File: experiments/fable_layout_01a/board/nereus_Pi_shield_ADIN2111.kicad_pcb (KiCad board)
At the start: 6 copper layers, 46 x 65 mm, 138 parts, among them J1 Raspberry_Pi_2_3, J5 SM02B-GHS-TB, T1 74930000, T2 74930000, U1 ADIN2111BCPZ, U10 LMR51430YDDCR, U11 TPS26621DRCR, U2 AP22913CN4-7, U3 AP22913CN4-7, U4 INA232AIDDFR, U5 LMR51430YDDCR, U6 TPS62840YBGR, Y1 ABM11W-25.0000MHZ-6-K1Z-T3

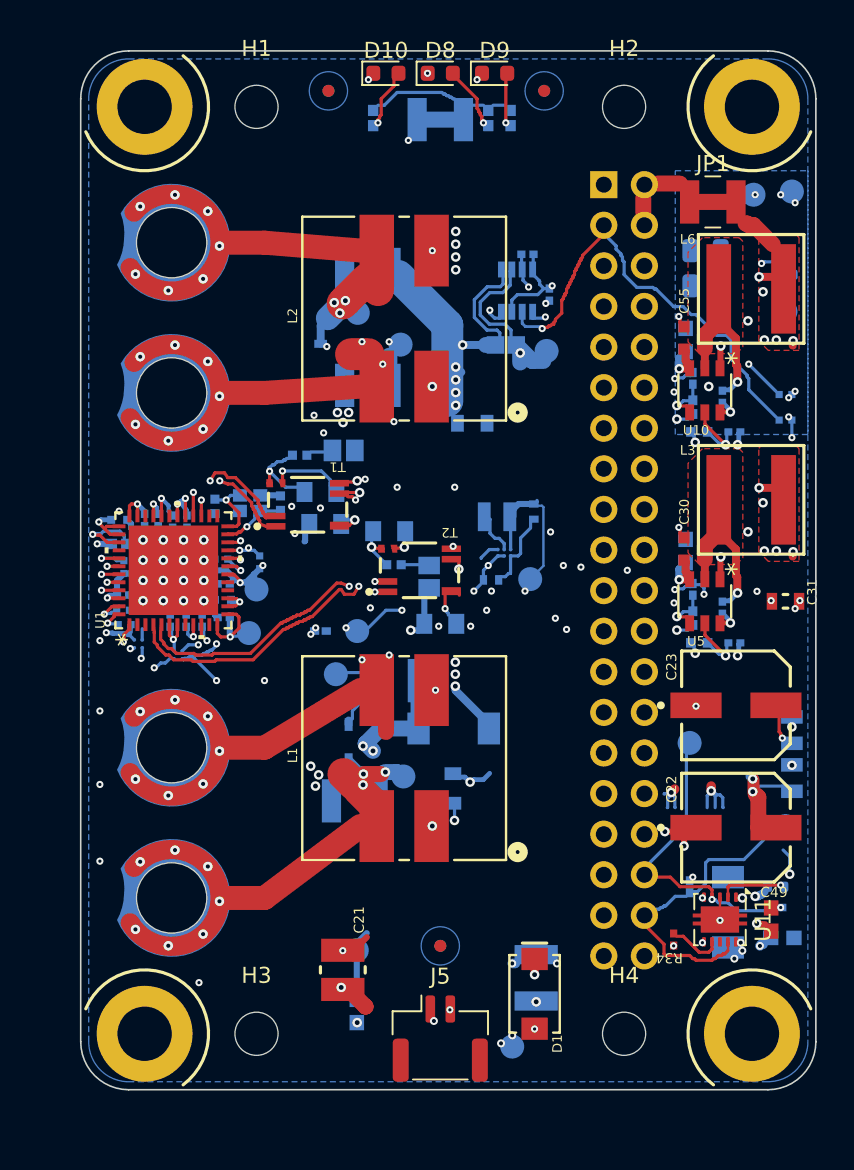
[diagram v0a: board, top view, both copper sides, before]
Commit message: fable layout 1.a S2.b: board 49 x 68 (width west, height south), inserts 1.5 mm nearer the wall, U1 pocket (centre tried in 8 trials: OPTIONS A3), SPI first on an Internal 2 lane, straightened pairs 9.39/8.77/19.93/20.61, jumpers on top at the north edge, JLCPCB DFM 30/31, DRC 109 (all Sofar's) / 70, review + before/after pages, REPORT
Co-Authored-By: Claude Fable 5.1 <noreply@anthropic.com>
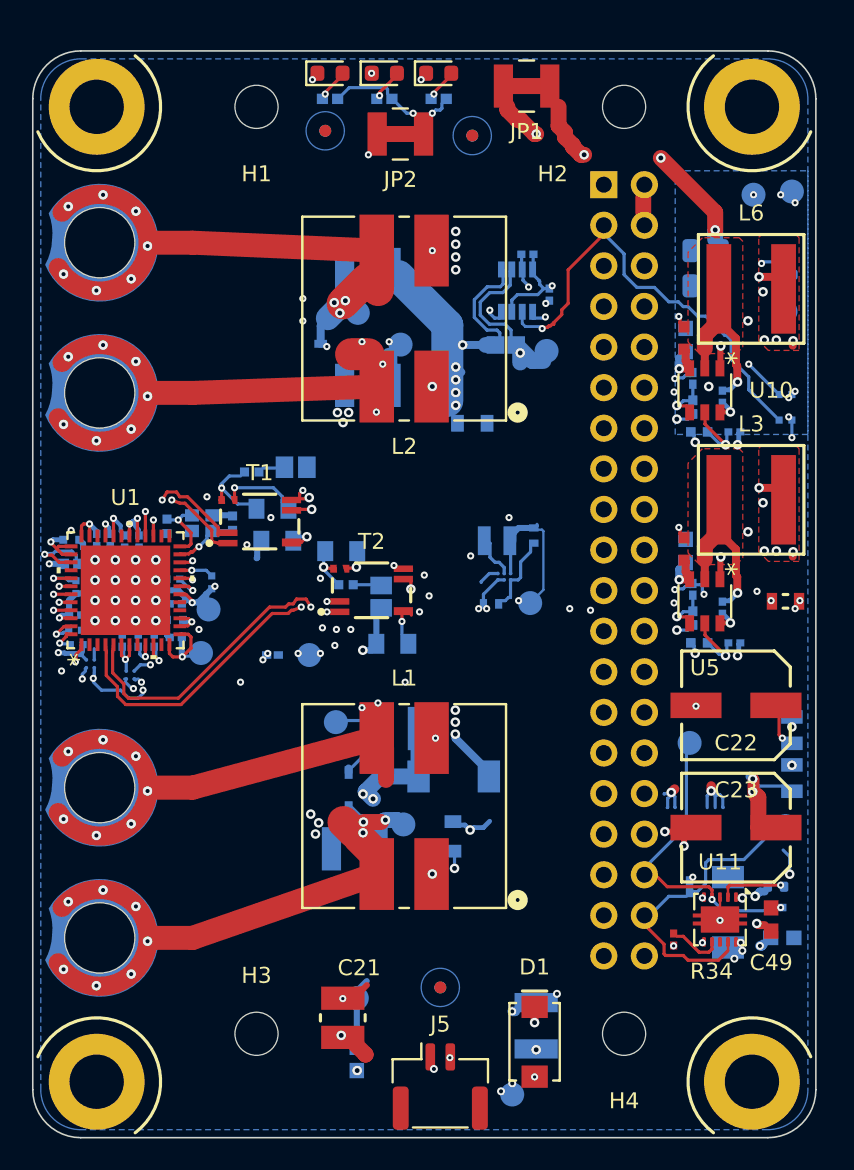
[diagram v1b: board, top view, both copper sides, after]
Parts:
- JP2: moved to F.Cu
- moved JP1 13.7 mm to (20.4, 2.20)
- moved R44 6.61 mm to (11.5, 3.00), turned to 0 degrees
- moved FID1 5.30 mm to (17.0, 5.30)
- moved FID3 5.30 mm to (17.0, 5.30)
- moved MP1 5.15 mm to (-6.31, 46.1)
- moved MP2 5.15 mm to (-6.31, 55.5)
- moved R45 4.66 mm to (14.9, 3.00), turned to 0 degrees
- moved MP3 4.50 mm to (-6.31, 12.0)
- moved MP4 4.50 mm to (-6.31, 21.4)
- moved MTG3 4.24 mm to (-6.50, 64.5)
- moved D10 3.50 mm to (8.10, 1.40)
- moved D8 3.50 mm to (11.5, 1.40)
- moved D9 3.50 mm to (14.9, 1.40)
- moved TP8 3.35 mm to (6.80, 37.8)
- moved R43 3.35 mm to (4.50, 37.8)
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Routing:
- net /Top-Level Schematic/~{ADIN_CS}: track 67.6 -> 42.4 mm, vias 6 -> 2
- net /Top-Level Schematic/ADIN_MISO: track 66.5 -> 41.9 mm, vias 1 -> 3
- net /Top-Level Schematic/5V_PI: track 9.13 -> 22.1 mm, vias 5 -> 8
- net /Top-Level Schematic/PI_5V: track 2.30 -> 11.2 mm, vias 0 -> 1
- net /Top-Level Schematic/BM1_P: track 39.1 -> 46.6 mm, vias 11 -> 10
- net /Top-Level Schematic/BM1_N: track 54.1 -> 61.3 mm
- net /Top-Level Schematic/BM2_N: track 34.6 -> 41.4 mm
- net /Top-Level Schematic/BM2_P: track 48.5 -> 54.1 mm
- net /Top-Level Schematic/~{ADIN_INT}: track 40.6 -> 44.8 mm
- net 3V3: track 112.3 -> 116.3 mm
- net /Top-Level Schematic/ADIN_SCK: track 32.3 -> 35.1 mm, vias 3 -> 1
- net /Top-Level Schematic/ADIN_MOSI: track 33.4 -> 35.9 mm, vias 2 -> 1
- net 1V8: track 37.0 -> 39.3 mm, vias 4 -> 3
- net Net-(D8-A): track 3.36 -> 1.33 mm
- net /Top-Level Schematic/BM2_DATA_N: track 18.6 -> 20.6 mm
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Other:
- board size 46 x 65 mm -> 49 x 68 mm
- board text added: "band y 26.5..37.5 (11 mm)"

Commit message: fable layout 1.a S2.b: QE round 3 fixes (no via in a solder pad: router padvia map, DFM rows 29/30 measured, small-pad 0.2 mm stubs per BRIEF 6, nits) + Nick's decisions from the renders (20 W inductor courtyard + 2 mm as the keep-out, U1 3 mm east); rebuilt from M0: pairs 9.39/8.77/20.19/20.87, DRC 109 (all Sofar's) / 68, DFM 30/31
Co-Authored-By: Claude Fable 5.1 <noreply@anthropic.com>
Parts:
- moved C6 3.00 mm to (-5.09, 30.6)
- moved TP8 3.00 mm to (9.80, 37.8)
- moved C4 3.00 mm to (-2.65, 30.6)
- moved C9 3.00 mm to (-1.90, 36.9)
- moved U2 3.00 mm to (-1.40, 39.0)
- moved U3 3.00 mm to (-3.90, 38.3)
- moved C1 3.00 mm to (-0.90, 36.9)
- moved C11 3.00 mm to (-0.85, 30.7)
- moved C12 3.00 mm to (-3.50, 30.6)
- moved C14 3.00 mm to (-4.85, 35.3)
- moved C16 3.00 mm to (7.50, 28.6)
- moved C18 3.00 mm to (7.80, 30.6)
- moved C24 3.00 mm to (11.8, 31.3)
- moved C25 3.00 mm to (15.0, 37.1)
- moved C27 3.00 mm to (14.3, 34.1)
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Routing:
- net 1V8: track 39.3 -> 34.6 mm
- net GND: track 54.1 -> 57.8 mm
- net Net-(U4-ALERT): track 5.20 -> 8.37 mm
- net /Top-Level Schematic/~{ADIN_RST}: track 30.0 -> 27.0 mm
- net /Top-Level Schematic/ADIN_MISO: track 41.9 -> 38.9 mm
- net /Top-Level Schematic/ADIN_MOSI: track 35.9 -> 33.0 mm
- net /Top-Level Schematic/ADIN_SCK: track 35.1 -> 32.2 mm
- net VBUS: track 28.9 -> 31.3 mm
- net 3V3: track 116.3 -> 113.9 mm, vias 21 -> 16
- net /Top-Level Schematic/PAYLOAD_EN: track 15.6 -> 18.0 mm
- net /Top-Level Schematic/~{ADIN_INT}: track 44.8 -> 42.6 mm, vias 1 -> 2
- net /Top-Level Schematic/~{ADIN_CS}: track 42.4 -> 40.4 mm
- net ADIN_VDDIO: track 49.1 -> 50.9 mm, vias 10 -> 6
- net /Top-Level Schematic/BM2_P: track 54.1 -> 55.8 mm
- net /Top-Level Schematic/BM2_N: track 41.4 -> 43.0 mm, vias 12 -> 10
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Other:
- board text added: "L1 SRF1260 courtyard 13.1 x 13.6 (20 W; +2 mm clear)"
- board text added: "L2 SRF1260 courtyard 13.1 x 13.6 (20 W; +2 mm clear)"
- board text added: "band y 25.55..38.45 (13 mm)"
- board text removed: "L1 50 W envelope 15.5 x 15.5 (+2 mm clear)"
- board text removed: "L2 50 W envelope 15.5 x 15.5 (+2 mm clear)"
- board text removed: "band y 26.5..37.5 (11 mm)"
